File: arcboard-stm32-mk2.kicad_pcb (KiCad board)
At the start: 2 copper layers, 60 x 60 mm, 90 parts, among them J1 Conn_01x04_Socket, J17 Conn_01x04_Socket, J2 Conn_01x04_Socket, J3 Conn_01x04_Socket, J4 Conn_01x02_Socket, J5 Conn_01x02_Socket, J6 Conn_01x02_Socket, J7 Conn_01x02_Socket, J8 Conn_01x02_Socket, U1 XC6210B332MR-G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

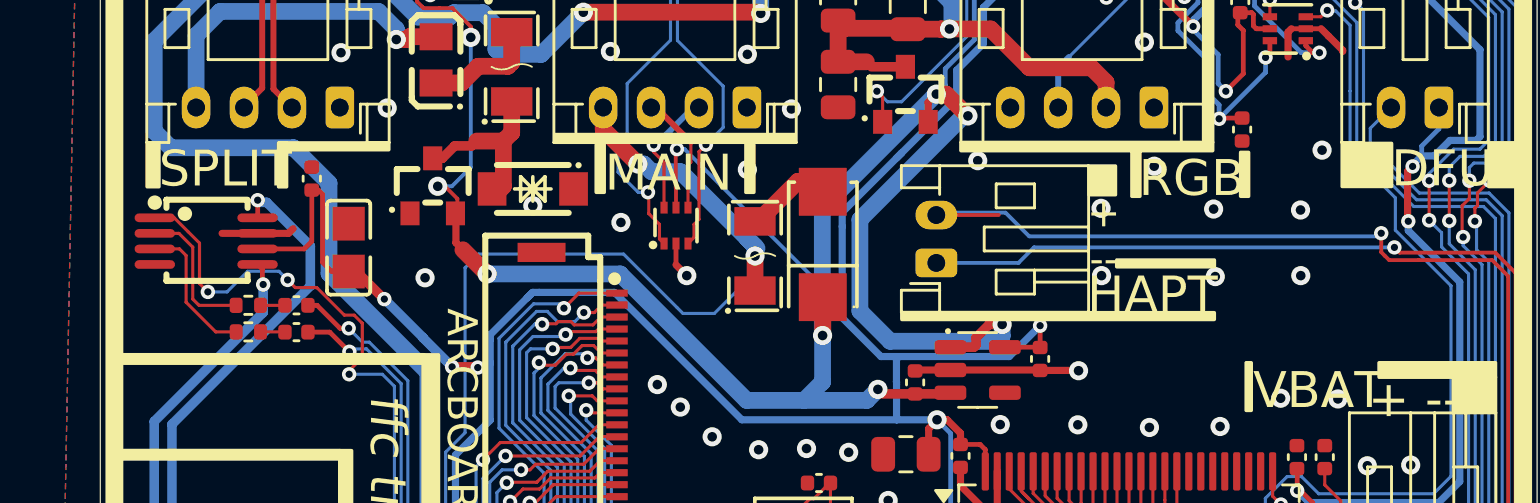
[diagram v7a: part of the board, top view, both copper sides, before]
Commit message: improved polyfuse part, fixing critical amplifier symbol mistake, other re-ordering
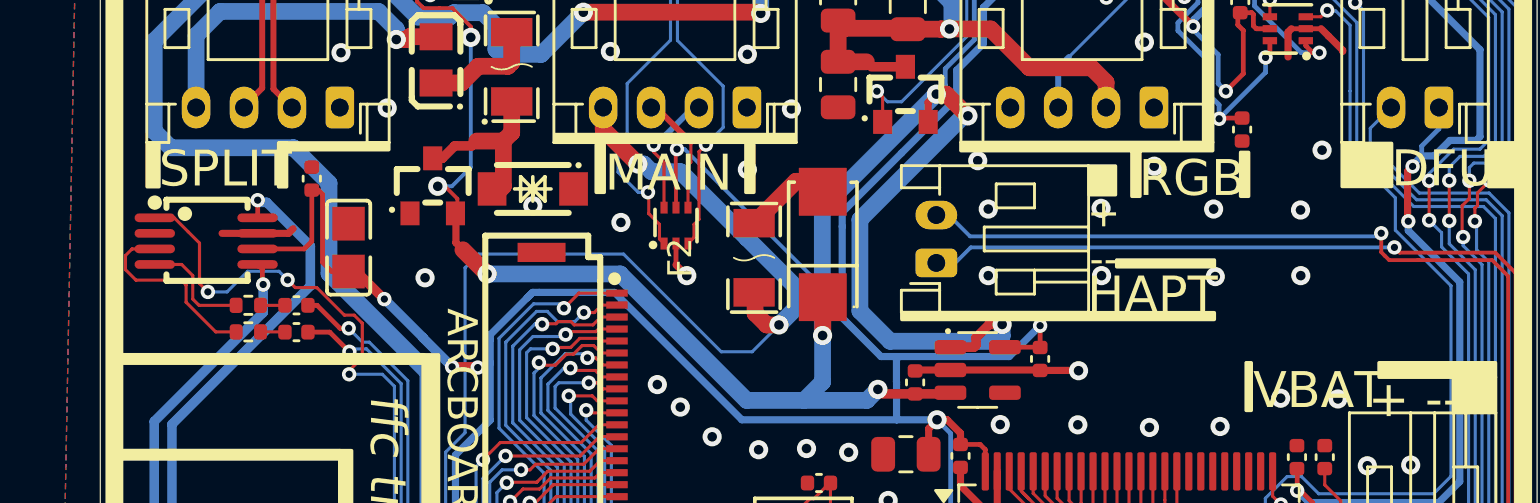
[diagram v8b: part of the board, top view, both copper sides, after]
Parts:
- removed F1: Polyfuse, kicad-libraries:F1206
- added F2: 1206L150SLYR, kicad-libraries:F1206, F.Cu at (97.3, 83.8)
- U2: value STM32F405VGTx -> STM32F407VGTx
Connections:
- U6 pad 2: Net-(U6-IN-) -> unconnected-(U6-NC-Pad2)
- U6 pad 4: (no net) -> Net-(U6-IN-)
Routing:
- net VBUS: track 125.4 -> 130.1 mm
- net HAPTIC_pos: track 69.8 -> 67.2 mm
- net Net-(U6-IN+): track 5.97 -> 8.05 mm
- net Net-(U6-IN-): track 5.91 -> 4.68 mm
- net GND: vias 65 -> 67
